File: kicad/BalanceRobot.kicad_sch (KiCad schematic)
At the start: 23 parts, among them J1 Stepper 1, J2 Stepper 2, J3 Conn_01x05, U1 TA48M05F, U2 LT1172, U3 M5Atom, U4 TB67S158NG

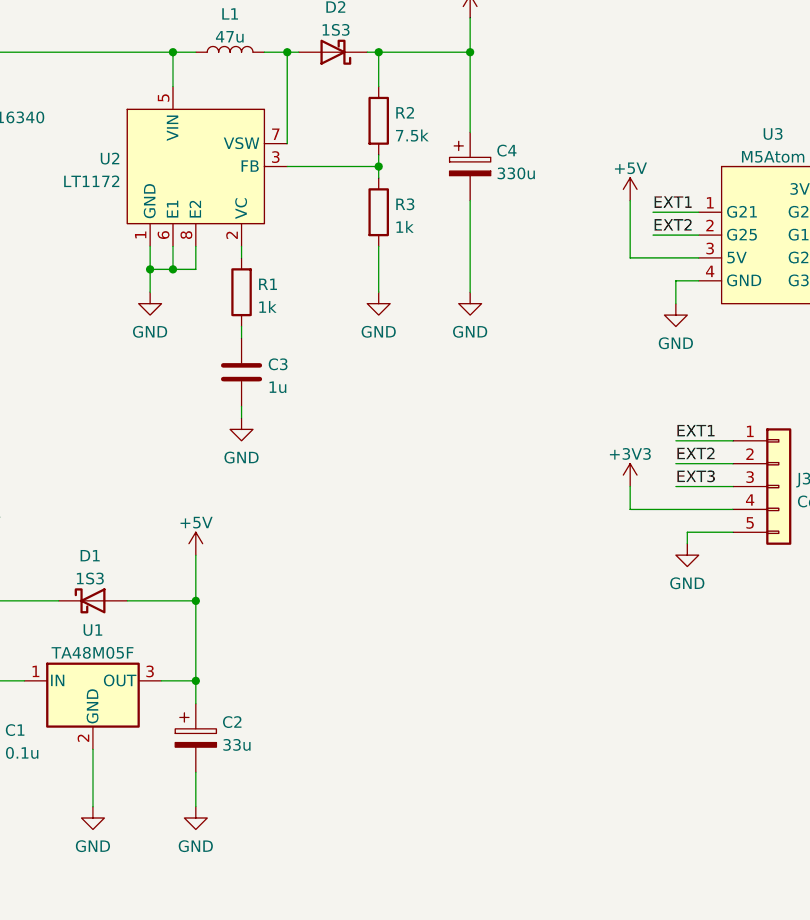
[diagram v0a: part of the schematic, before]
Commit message: Update schematic to reflect actual values
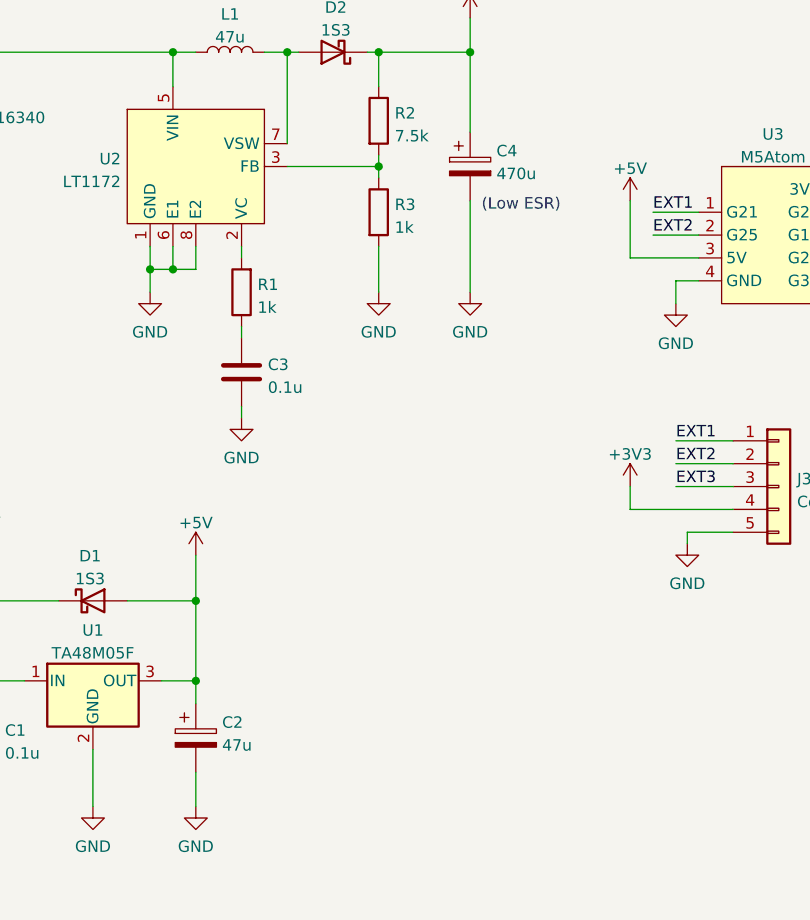
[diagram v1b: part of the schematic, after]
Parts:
- C2: value 33u -> 47u
- C3: value 1u -> 0.1u
- C4: value 330u -> 470u
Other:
- note added: "(Low ESR)"
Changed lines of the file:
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@@
     (stroke (width 0) (type default) (color 0 0 0 0))
+  )
+  (text "(Low ESR)" (at 106.68 92.71 0)
+    (effects (font (size 1.27 1.27)) (justify left bottom))
   )
   (label "LATCH" (at 172.72 86.36 0)
@@
       (effects (font (size 1.27 1.27)) (justify left))
     )
-    (property "Value" "33u" (id 1) (at 77.851 151.9432 0)
+    (property "Value" "47u" (id 1) (at 77.851 151.9432 0)
       (effects (font (size 1.27 1.27)) (justify left))
     )
@@
       (effects (font (size 1.27 1.27)) (justify left))
     )
-    (property "Value" "330u" (id 1) (at 108.331 88.4432 0)
+    (property "Value" "470u" (id 1) (at 108.331 88.4432 0)
       (effects (font (size 1.27 1.27)) (justify left))
     )
@@
       (effects (font (size 1.27 1.27)) (justify left))
     )
-    (property "Value" "1u" (id 1) (at 82.931 112.1922 0)
+    (property "Value" "0.1u" (id 1) (at 82.931 112.1922 0)
       (effects (font (size 1.27 1.27)) (justify left))
     )
@@
     )
     (path "/465896ee-e1d0-442e-8bde-8fac50910dfd"
-      (reference "C2") (unit 1) (value "33u") (footprint "Capacitor_THT:CP_Radial_D5.0mm_P2.50mm")
+      (reference "C2") (unit 1) (value "47u") (footprint "Capacitor_THT:CP_Radial_D5.0mm_P2.50mm")
     )
     (path "/e8656200-ac1c-4b4f-85dd-c2aaa0406e1e"
-      (reference "C3") (unit 1) (value "1u") (footprint "Capacitor_THT:C_Disc_D3.0mm_W1.6mm_P2.50mm")
+      (reference "C3") (unit 1) (value "0.1u") (footprint "Capacitor_THT:C_Disc_D3.0mm_W1.6mm_P2.50mm")
     )
     (path "/dd589c3e-1a73-40e3-b0dc-96c44ecf7431"
-      (reference "C4") (unit 1) (value "330u") (footprint "Capacitor_THT:CP_Radial_D8.0mm_P5.00mm")
+      (reference "C4") (unit 1) (value "470u") (footprint "Capacitor_THT:CP_Radial_D8.0mm_P5.00mm")
     )
     (path "/daee85e0-2341-48ca-a66d-285e2859aad2"
